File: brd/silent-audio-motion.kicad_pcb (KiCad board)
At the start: 2 copper layers, 70 x 50 mm, 80 parts, among them J1 AUDIO_IN, J2 ISP, J3 UART, J4 OUT_L, J5 OUT_R, J8 POWER, Q1 DMP2040, U1 MCP6004, U2 ATMEGA328P-AU, U3 TB6612FNG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

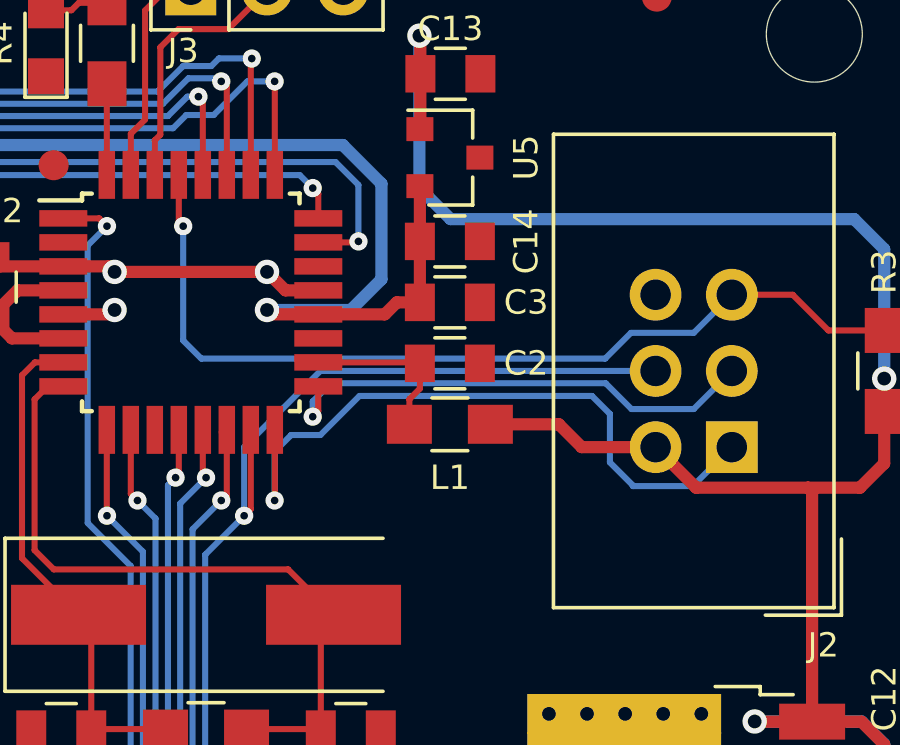
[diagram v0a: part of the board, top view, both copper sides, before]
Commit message: corregido problema con referencia analogica
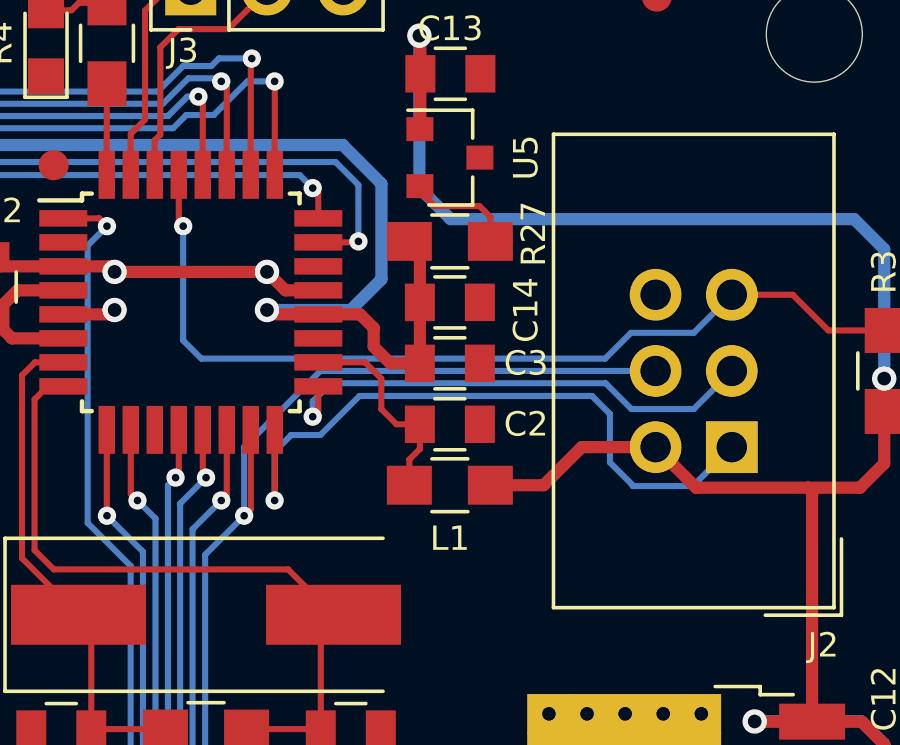
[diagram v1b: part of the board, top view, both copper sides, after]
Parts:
- added R27: 220R, Resistors_SMD:R_0805_HandSoldering, F.Cu at (54.1, 10.2)
- moved C14 2.03 mm to (54.1, 12.2)
- moved C2 2.03 mm to (54.1, 16.3)
- moved C3 2.03 mm to (54.1, 14.2)
- moved L1 2.03 mm to (54.1, 18.3)
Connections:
- U5 pad 2: VDDA -> Net-(R27-Pad2)
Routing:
- net Net-(R27-Pad2): track 0.00 -> 3.69 mm
- net Net-(C2-Pad1): track 5.58 -> 7.01 mm
- net VDDA: track 78.3 -> 79.5 mm
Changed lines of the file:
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@@
 (kicad_pcb (version 4) (host pcbnew 4.0.7-e2-6376~61~ubuntu18.04.1)
   (general
-    (links 0)
-    (no_connects 0)
-    (area 100.466001 61.484 194.248572 128.983001)
+    (links 202)
+    (no_connects 2)
+    (area -0.075001 -0.075001 70.075001 50.075001)
     (thickness 1.6)
     (drawings 22)
-    (tracks 655)
+    (tracks 666)
     (zones 0)
-    (modules 80)
-    (nets 62)
+    (modules 81)
+    (nets 63)
   )
   (page A4)
@@
   (net 60 "Net-(J5-Pad1)")
   (net 61 "Net-(J5-Pad2)")
+  (net 62 "Net-(R27-Pad2)")
   (net_class Default "This is the default net class."
     (clearance 0.2032)
@@
     (add_net "Net-(R21-Pad1)")
     (add_net "Net-(R26-Pad2)")
+    (add_net "Net-(R27-Pad2)")
     (add_net "Net-(R4-Pad2)")
     (add_net "Net-(U2-Pad11)")
@@
       (net 3 +5V))
     (pad 2 smd rect (at -1 0.95) (size 0.9 0.8) (layers F.Cu F.Paste F.Mask)
-      (net 4 VDDA))
+      (net 62 "Net-(R27-Pad2)"))
     (pad 3 smd rect (at 1 0) (size 0.9 0.8) (layers F.Cu F.Paste F.Mask)
       (net 1 GND))
@@
   )
   (module Capacitors_SMD:C_0805 (layer F.Cu)
-    (at 54.102 14.224)
+    (at 54.102 16.256)
     (descr "Capacitor SMD 0805, reflow soldering, AVX (see smccp.pdf)")
     (tags "capacitor 0805")
@@
   )
   (module Capacitors_SMD:C_0805 (layer F.Cu)
-    (at 54.102 12.192)
+    (at 54.102 14.224)
     (descr "Capacitor SMD 0805, reflow soldering, AVX (see smccp.pdf)")
     (tags "capacitor 0805")
@@
   )
   (module Capacitors_SMD:C_0805 (layer F.Cu)
-    (at 54.102 10.16)
+    (at 54.102 12.192)
     (descr "Capacitor SMD 0805, reflow soldering, AVX (see smccp.pdf)")
     (tags "capacitor 0805")
     (attr smd)
-    (fp_text reference C14 (at 2.54 0 90) (layer F.SilkS)
+    (fp_text reference C14 (at 2.54 0.254 90) (layer F.SilkS)
       (effects (font (size 0.8128 0.8128) (thickness 0.1524)))
     )
@@
   )
   (module Inductors_SMD:L_0805_HandSoldering (layer F.Cu)
-    (at 54.102 16.256)
+    (at 54.102 18.288)
     (descr "Resistor SMD 0805, hand soldering")
     (tags "resistor 0805")
@@
       (xy 4.628444 2.554111)) (layer B.SilkS) (width 0.01))
   )
-  (gr_text "TRG R" (at 6.858 8.382 360) (layer B.SilkS)
+  (module Resistors_SMD:R_0805_HandSoldering (layer F.Cu)
+    (at 54.102 10.16)
+    (descr "Resistor SMD 0805, hand soldering")
+    (tags "resistor 0805")
+    (attr smd)
+    (fp_text reference R27 (at 2.794 -0.254 90) (layer F.SilkS)
+      (effects (font (size 0.8128 0.8128) (thickness 0.1524)))
+    )
+    (fp_text value 220R (at -2.794 0) (layer F.Fab)
+      (effects (font (size 0.8128 0.8128) (thickness 0.1524)))
+    )
+    (fp_text user %R (at 0 0) (layer F.Fab)
+      (effects (font (size 0.508 0.508) (thickness 0.0762)))
+    )
+    (fp_line (start -1 0.62) (end -1 -0.62) (layer F.Fab) (width 0.1))
+    (fp_line (start 1 0.62) (end -1 0.62) (layer F.Fab) (width 0.1))
+    (fp_line (start 1 -0.62) (end 1 0.62) (layer F.Fab) (width 0.1))
+    (fp_line (start -1 -0.62) (end 1 -0.62) (layer F.Fab) (width 0.1))
+    (fp_line (start 0.6 0.88) (end -0.6 0.88) (layer F.SilkS) (width 0.12))
+    (fp_line (start -0.6 -0.88) (end 0.6 -0.88) (layer F.SilkS) (width 0.12))
+    (fp_line (start -2.35 -0.9) (end 2.35 -0.9) (layer F.CrtYd) (width 0.05))
+    (fp_line (start -2.35 -0.9) (end -2.35 0.9) (layer F.CrtYd) (width 0.05))
+    (fp_line (start 2.35 0.9) (end 2.35 -0.9) (layer F.CrtYd) (width 0.05))
+    (fp_line (start 2.35 0.9) (end -2.35 0.9) (layer F.CrtYd) (width 0.05))
+    (pad 1 smd rect (at -1.35 0) (size 1.5 1.3) (layers F.Cu F.Paste F.Mask)
+      (net 4 VDDA))
+    (pad 2 smd rect (at 1.35 0) (size 1.5 1.3) (layers F.Cu F.Paste F.Mask)
+      (net 62 "Net-(R27-Pad2)"))
+    (model ${KISYS3DMOD}/Resistors_SMD.3dshapes/R_0805.wrl
+      (at (xyz 0 0 0))
+      (scale (xyz 1 1 1))
+      (rotate (xyz 0 0 0))
+    )
+  )
+  (gr_text "TRG R" (at 6.858 8.382) (layer B.SilkS)
     (effects (font (size 1.5 1.5) (thickness 0.3)) (justify mirror))
   )
-  (gr_text "TRG L" (at 6.858 39.624 360) (layer B.SilkS)
+  (gr_text "TRG L" (at 6.858 39.624) (layer B.SilkS)
     (effects (font (size 1.5 1.5) (thickness 0.3)) (justify mirror))
   )
-  (gr_text "ADJ R" (at 6.858 18.796 360) (layer B.SilkS)
+  (gr_text "ADJ R" (at 6.858 18.796) (layer B.SilkS)
     (effects (font (size 1.5 1.5) (thickness 0.3)) (justify mirror))
   )
-  (gr_text "ADJ L" (at 6.858 29.21 360) (layer B.SilkS)
+  (gr_text "ADJ L" (at 6.858 29.21) (layer B.SilkS)
     (effects (font (size 1.5 1.5) (thickness 0.3)) (justify mirror))
   )
@@
   (segment (start 59.309 33.368) (end 60.579 33.368) (width 0.4064) (layer F.Cu) (net 2))
   (segment (start 55.56 34.052) (end 56.052 34.052) (width 0.25) (layer F.Cu) (net 2))
-  (segment (start 55.452 16.256) (end 57.734127 16.256) (width 0.4064) (layer F.Cu) (net 3))
-  (segment (start 57.734127 16.256) (end 58.496127 17.018) (width 0.4064) (layer F.Cu) (net 3))
+  (segment (start 58.496127 17.018) (end 57.226127 18.288) (width 0.4064) (layer F.Cu) (net 3))
+  (segment (start 57.226127 18.288) (end 55.452 18.288) (width 0.4064) (layer F.Cu) (net 3))
   (segment (start 58.496127 17.018) (end 60.96 17.018) (width 0.4064) (layer F.Cu) (net 3))
   (segment (start 15.494 22.606) (end 15.494 25.461244) (width 0.4064) (layer B.Cu) (net 3))
@@
   (segment (start 66.176 26.168) (end 67.824 26.168) (width 0.4064) (layer F.Cu) (net 3))
   (segment (start 44.237 31.452) (end 44.237 32.507405) (width 0.3302) (layer F.Cu) (net 3))
+  (segment (start 49.716 12.592) (end 51.109135 12.592) (width 0.4064) (layer F.Cu) (net 4))
+  (segment (start 51.109135 12.592) (end 51.562 13.044865) (width 0.4064) (layer F.Cu) (net 4))
+  (segment (start 51.562 13.044865) (end 51.562 13.669183) (width 0.4064) (layer F.Cu) (net 4))
+  (segment (start 52.116817 14.224) (end 53.102 14.224) (width 0.4064) (layer F.Cu) (net 4))
+  (segment (start 51.562 13.669183) (end 52.116817 14.224) (width 0.4064) (layer F.Cu) (net 4))
+  (segment (start 53.102 12.192) (end 53.102 10.51) (width 0.4064) (layer F.Cu) (net 4))
+  (segment (start 53.102 10.51) (end 52.752 10.16) (width 0.4064) (layer F.Cu) (net 4))
+  (segment (start 53.102 14.224) (end 53.102 12.192) (width 0.4064) (layer F.Cu) (net 4))
   (segment (start 12.7 25.4) (end 12.7 21.352456) (width 0.4064) (layer B.Cu) (net 4))
   (segment (start 16.166825 20.475762) (end 17.818436 18.824151) (width 0.4064) (layer B.Cu) (net 4))
@@
   (segment (start 48.152 12.592) (end 48.006 12.446) (width 0.4064) (layer F.Cu) (net 4))
   (via (at 48.006 12.446) (size 0.8128) (drill 0.4572) (layers F.Cu B.Cu) (net 4))
-  (segment (start 49.716 12.592) (end 51.932956 12.592) (width 0.4064) (layer F.Cu) (net 4))
-  (segment (start 51.932956 12.592) (end 52.332956 12.192) (width 0.4064) (layer F.Cu) (net 4))
-  (segment (start 52.332956 12.192) (end 53.102 12.192) (width 0.4064) (layer F.Cu) (net 4))
-  (segment (start 53.102 10.16) (end 53.102 8.316) (width 0.4064) (layer F.Cu) (net 4))
-  (segment (start 53.102 12.192) (end 53.102 10.16) (width 0.4064) (layer F.Cu) (net 4))
   (segment (start 41.216 14.192) (end 40.269829 14.192) (width 0.2032) (layer F.Cu) (net 7))
   (segment (start 39.839781 14.622048) (end 39.839781 20.721781) (width 0.2032) (layer F.Cu) (net 7))
@@
   (segment (start 41.962 40.934555) (end 39.704 43.192555) (width 0.4064) (layer F.Cu) (net 52))
   (segment (start 39.704 43.192555) (end 39.704 45.72) (width 0.4064) (layer F.Cu) (net 52))
-  (segment (start 53.102 14.224) (end 53.102 15.068315) (width 0.2032) (layer F.Cu) (net 53))
-  (segment (start 53.102 15.068315) (end 52.752 15.418315) (width 0.2032) (layer F.Cu) (net 53))
-  (segment (start 52.752 15.418315) (end 52.752 16.256) (width 0.2032) (layer F.Cu) (net 53))
-  (segment (start 49.716 14.192) (end 53.07 14.192) (width 0.2032) (layer F.Cu) (net 53))
-  (segment (start 53.07 14.192) (end 53.102 14.224) (width 0.2032) (layer F.Cu) (net 53))
+  (segment (start 52.752 18.288) (end 52.752 17.427639) (width 0.2032) (layer F.Cu) (net 53))
+  (segment (start 52.752 17.427639) (end 53.102 17.077639) (width 0.2032) (layer F.Cu) (net 53))
+  (segment (start 53.102 17.077639) (end 53.102 16.256) (width 0.2032) (layer F.Cu) (net 53))
+  (segment (start 49.716 14.192) (end 51.276 14.192) (width 0.2032) (layer F.Cu) (net 53))
+  (segment (start 51.276 14.192) (end 51.816 14.732) (width 0.2032) (layer F.Cu) (net 53))
+  (segment (start 51.816 14.732) (end 51.816 15.748) (width 0.2032) (layer F.Cu) (net 53))
+  (segment (start 51.816 15.748) (end 52.324 16.256) (width 0.2032) (layer F.Cu) (net 53))
+  (segment (start 52.324 16.256) (end 53.102 16.256) (width 0.2032) (layer F.Cu) (net 53))
   (segment (start 41.216 14.992) (end 40.691486 14.992) (width 0.2032) (layer F.Cu) (net 54))
   (segment (start 48.710571 21.092571) (end 50.224 22.606) (width 0.2032) (layer F.Cu) (net 54))
@@
   (segment (start 49.302079 41.682079) (end 54.015633 41.682079) (width 0.4064) (layer F.Cu) (net 61))
   (segment (start 54.015633 41.682079) (end 54.864 42.530446) (width 0.4064) (layer F.Cu) (net 61))
+  (segment (start 53.102 8.316) (end 53.102 8.490303) (width 0.2032) (layer F.Cu) (net 62))
+  (segment (start 53.102 8.490303) (end 53.594 8.982303) (width 0.2032) (layer F.Cu) (net 62))
+  (segment (start 53.594 8.982303) (end 55.089139 8.982303) (width 0.2032) (layer F.Cu) (net 62))
+  (segment (start 55.089139 8.982303) (end 55.452 9.345164) (width 0.2032) (layer F.Cu) (net 62))
+  (segment (start 55.452 9.345164) (end 55.452 10.16) (width 0.2032) (layer F.Cu) (net 62))
   (zone (net 1) (net_name GND) (layer F.Cu) (hatch edge 0.508)
     (connect_pads (clearance 0.254))

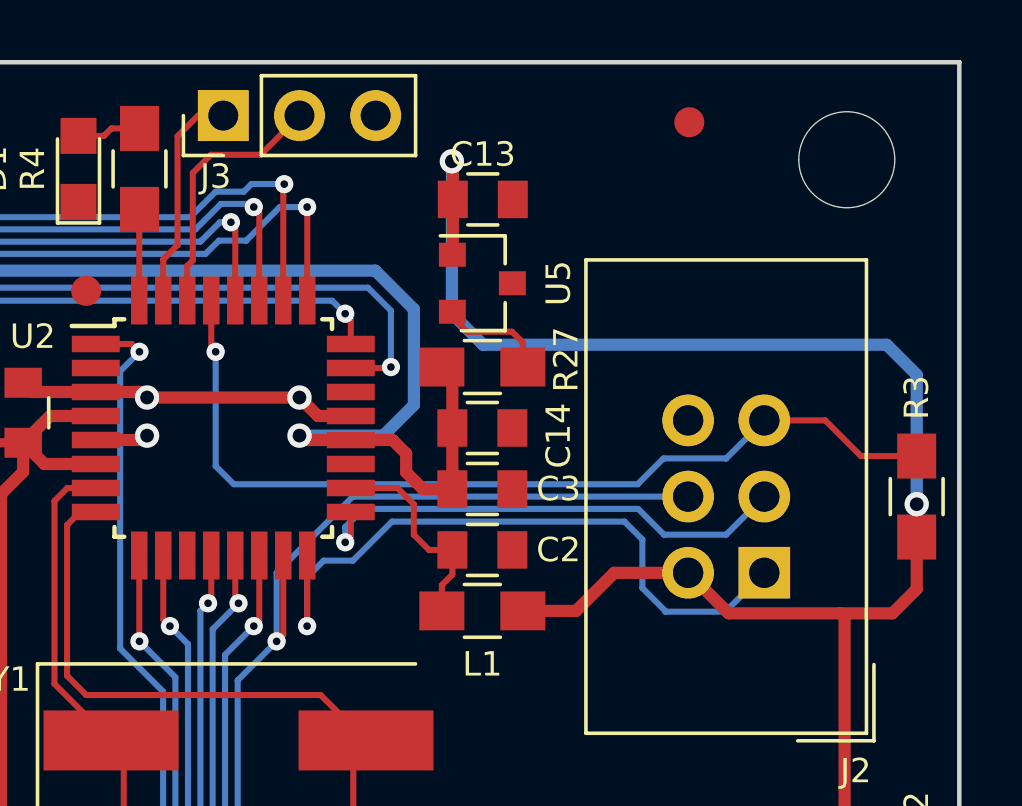
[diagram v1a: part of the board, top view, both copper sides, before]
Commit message: añadido pin DTR para reset en cabecera UART
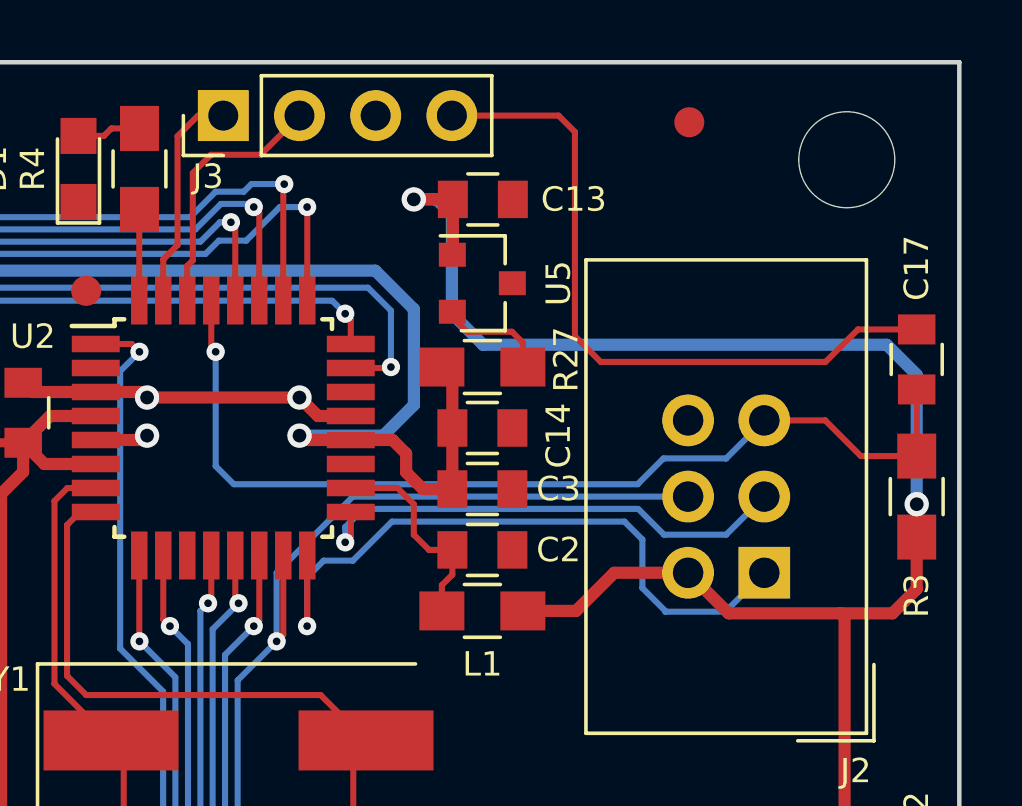
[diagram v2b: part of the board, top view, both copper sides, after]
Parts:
- added C17: 100nF, Capacitors_SMD:C_0805, F.Cu at (68.6, 9.91)
- J3: footprint Pin_Headers:Pin_Header_Straight_1x03_Pitch2.54mm -> Pin_Headers:Pin_Header_Straight_1x04_Pitch2.54mm
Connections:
- net Net-(J2-Pad5) renamed /~RST
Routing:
- net Net-(C17-Pad1): track 0.00 -> 23.3 mm
- net /~RST: track 30.6 -> 32.8 mm
